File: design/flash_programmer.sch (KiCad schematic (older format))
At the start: 27 parts, among them P1 ISP, U1 MAX662A, U2 2N3906, U3 ATMEGA328P_TQFN, U4 GLS27SF010, U5 74HC595, U6 74HC595

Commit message: Redo PCB: fix errors and shrink
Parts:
- removed R6, R8: 10k, Resistors_SMD:R_0805_HandSoldering, symbol R
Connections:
- net labels added: UNUSED_GND
- wire segments 170 -> 163
- no-connect marks 1 -> 2
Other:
- moved on the sheet: R1, R7

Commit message: Work in progress: Add `12V capability to A9
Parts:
- removed C1, C2: 22nF, Capacitors_SMD:C_0805_HandSoldering, symbol C
- removed C3, C5: 4.7uF, Capacitors_SMD:C_0805_HandSoldering, symbol C
- removed C8: 120nF, Capacitors_SMD:C_0805_HandSoldering, symbol C
- removed D1: LED, LEDs:LED_0805, symbol LED
- removed R2: 150, Resistors_SMD:R_0805_HandSoldering, symbol R
- removed R4: 10k, Resistors_SMD:R_0805_HandSoldering, symbol R
- removed U1: MAX662A, Housings_SOIC:SOIC-8_3.9x4.9mm_Pitch1.27mm, symbol MAX662A
- removed U2: 2N3906, TO_SOT_Packages_SMD:SOT-23_Handsoldering, symbol 2N3906
- removed U4: GLS27SF010, Housings_DIP:DIP-32_W15.24mm, symbol GLS27SF010
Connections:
- net labels added: D[0..7]
- net labels removed: VPP
- wire segments 163 -> 100
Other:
- note removed: "12V Step Up Voltage Supply"
- note removed: "Bypass capacitors for GLS27SF010"
- note removed: "Bypass capacitors for MAX662A"
- note removed: "Flash ROM under read/write"
- note removed: "Write indicator light"
- moved on the sheet: D2, P1, R3

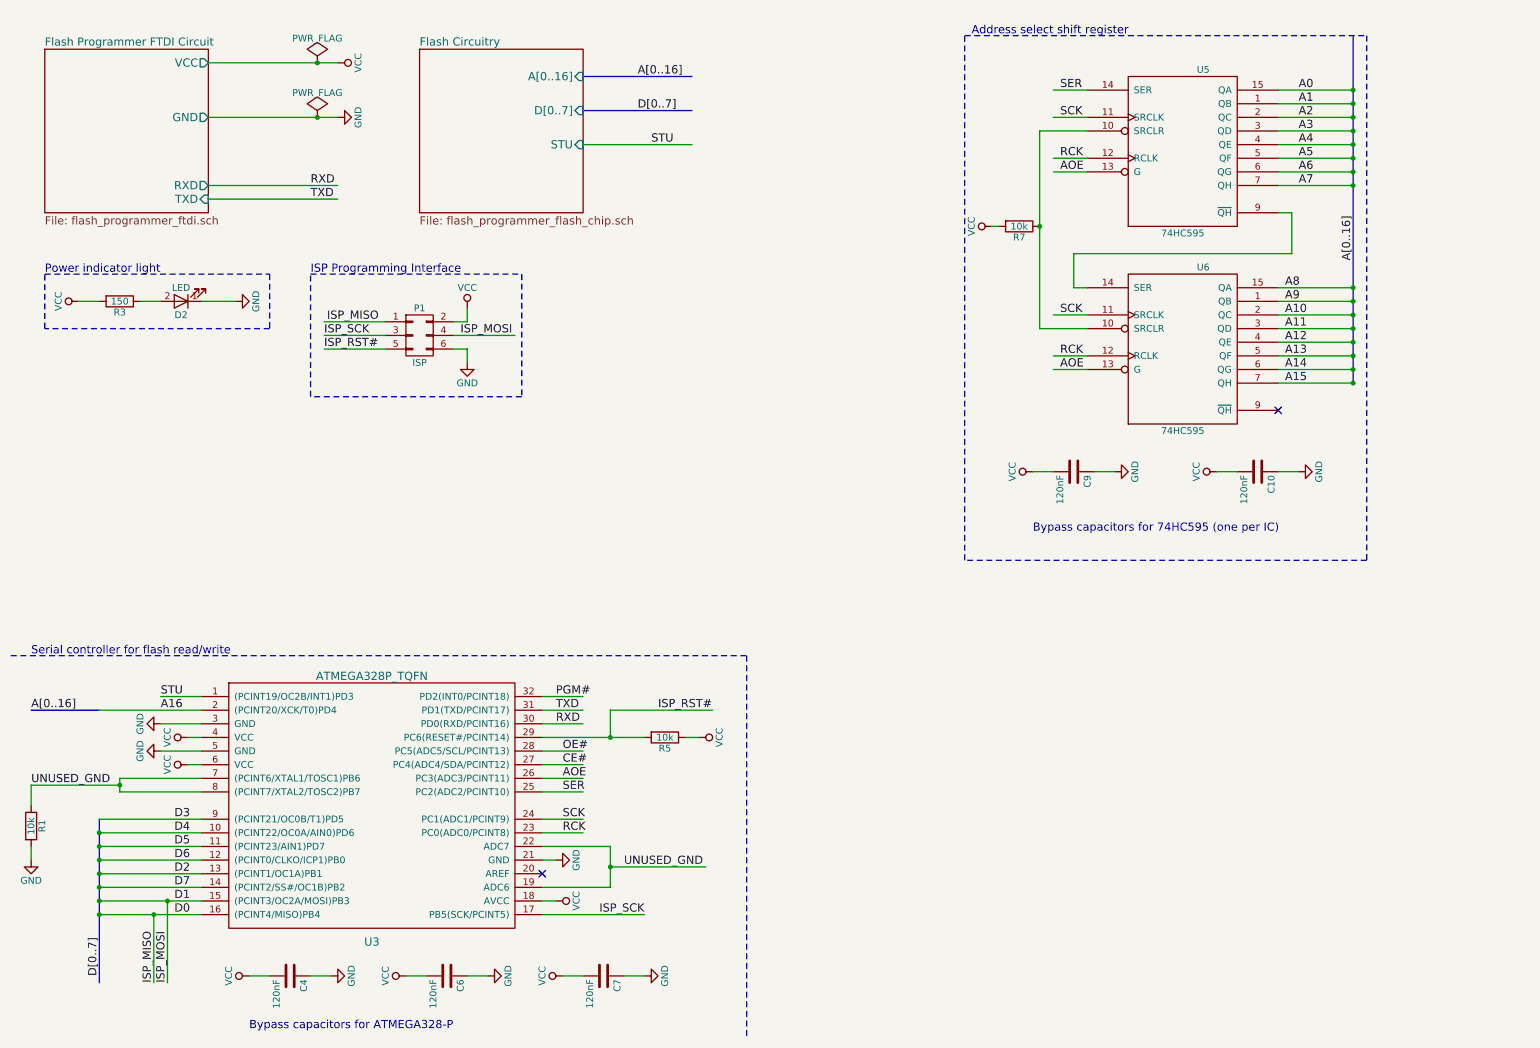
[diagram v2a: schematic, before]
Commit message: Redo the A9_P circuit with a P-channel MOSFET to avoid voltage drop
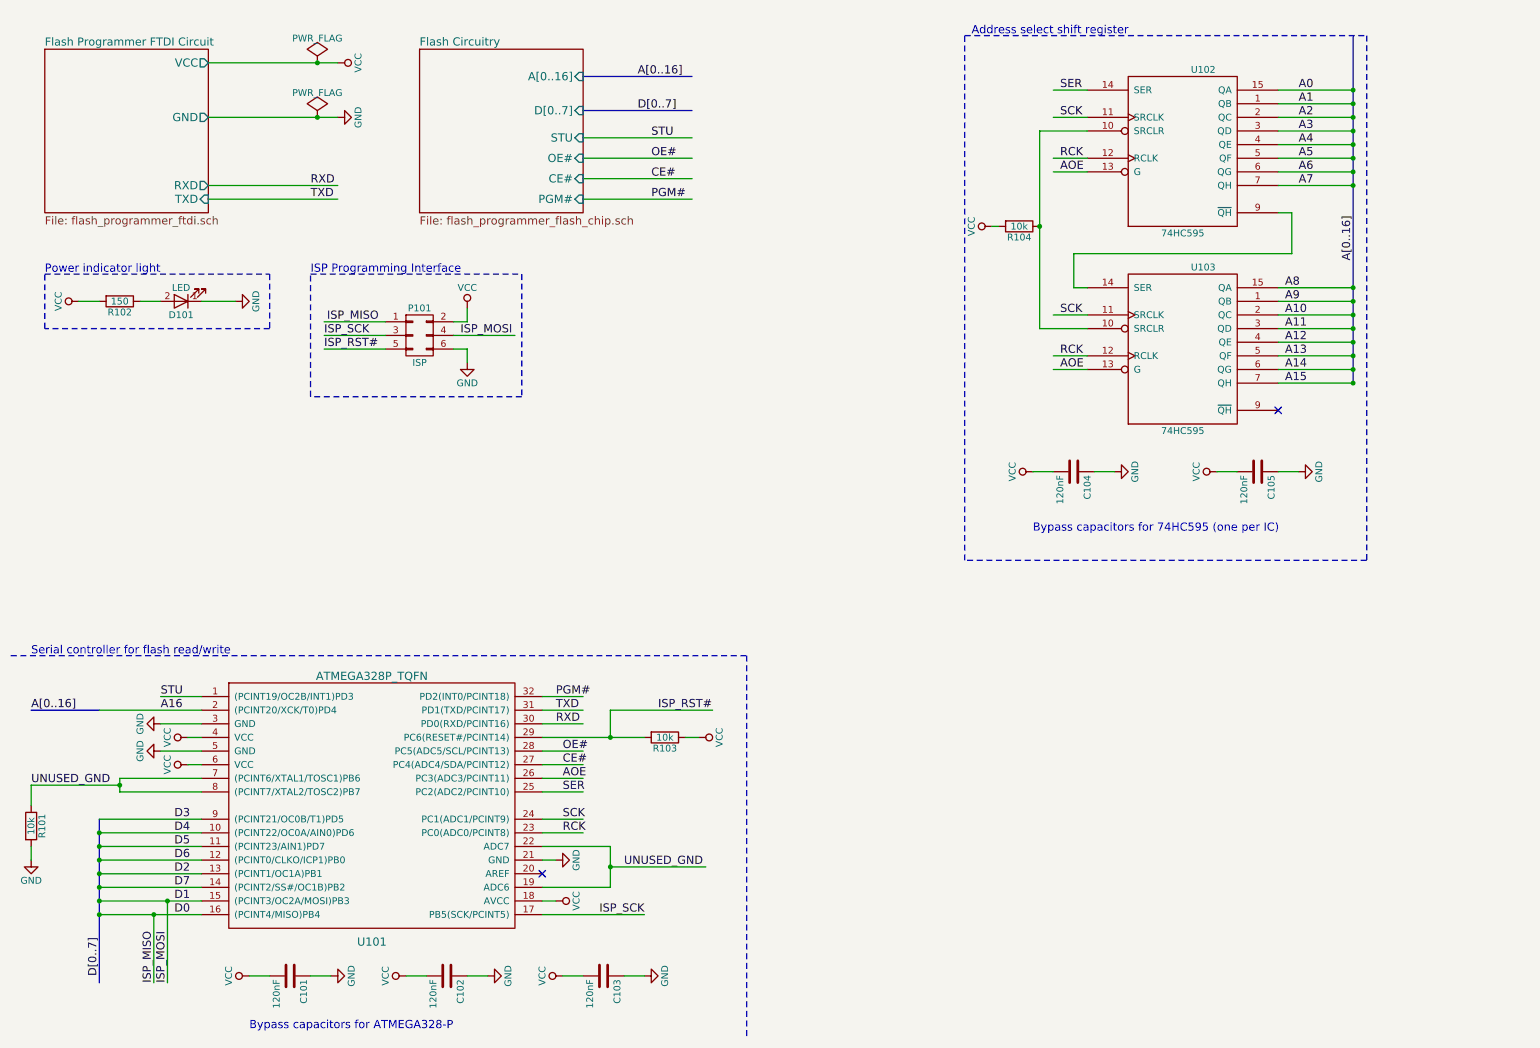
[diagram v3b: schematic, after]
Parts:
- renumbered C4 to C101, C6 to C102, C7 to C103, C9 to C104, C10 to C105, D2 to D101, P1 to P101, R1 to R101, R3 to R102, R5 to R103, R7 to R104, U3 to U101, U5 to U102, U6 to U103
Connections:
- wire segments 100 -> 103
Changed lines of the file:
@@
 $EndDescr
 $Comp
-L 74HC595 U5
+L 74HC595 U102
 U 1 1 5861865E
 P 9100 1500
-F 0 "U5" H 9250 2100 50  0000 C CNN
+F 0 "U102" H 9250 2100 50  0000 C CNN
 F 1 "74HC595" H 9100 900 50  0000 C CNN
 F 2 "Housings_SOIC:SOIC-16_3.9x9.9mm_Pitch1.27mm" H 9100 1500 50  0001 C CNN
@@
 $EndComp
 $Comp
-L 74HC595 U6
+L 74HC595 U103
 U 1 1 586186AF
 P 9100 2950
-F 0 "U6" H 9250 3550 50  0000 C CNN
+F 0 "U103" H 9250 3550 50  0000 C CNN
 F 1 "74HC595" H 9100 2350 50  0000 C CNN
 F 2 "Housings_SOIC:SOIC-16_3.9x9.9mm_Pitch1.27mm" H 9100 2950 50  0001 C CNN
@@
 RXD
 $Comp
-L C C4
+L C C101
 U 1 1 5861E696
 P 2550 7550
-F 0 "C4" H 2575 7650 50  0000 L CNN
+F 0 "C101" H 2575 7650 50  0000 L CNN
 F 1 "120nF" H 2575 7450 50  0000 L CNN
 F 2 "Capacitors_SMD:C_0805_HandSoldering" H 2588 7400 50  0001 C CNN
@@
 $EndComp
 $Comp
-L C C6
+L C C102
 U 1 1 5861E6C9
 P 3700 7550
-F 0 "C6" H 3725 7650 50  0000 L CNN
+F 0 "C102" H 3725 7650 50  0000 L CNN
 F 1 "120nF" H 3725 7450 50  0000 L CNN
 F 2 "Capacitors_SMD:C_0805_HandSoldering" H 3738 7400 50  0001 C CNN
@@
 RCK
 $Comp
-L R R7
+L R R104
 U 1 1 58622531
 P 7900 2050
-F 0 "R7" V 7980 2050 50  0000 C CNN
+F 0 "R104" V 7980 2050 50  0000 C CNN
 F 1 "10k" V 7900 2050 50  0000 C CNN
 F 2 "Resistors_SMD:R_0805_HandSoldering" V 7830 2050 50  0001 C CNN
@@
 A15
 $Comp
-L R R5
+L R R103
 U 1 1 58627FBC
 P 5300 5800
-F 0 "R5" V 5380 5800 50  0000 C CNN
+F 0 "R103" V 5380 5800 50  0000 C CNN
 F 1 "10k" V 5300 5800 50  0000 C CNN
 F 2 "Resistors_SMD:R_0805_HandSoldering" V 5230 5800 50  0001 C CNN
@@
 Connection ~ 10350 2600
 $Comp
-L C C9
+L C C104
 U 1 1 58633F2E
 P 8300 3850
-F 0 "C9" H 8325 3950 50  0000 L CNN
+F 0 "C104" H 8325 3950 50  0000 L CNN
 F 1 "120nF" H 8325 3750 50  0000 L CNN
 F 2 "Capacitors_SMD:C_0805_HandSoldering" H 8338 3700 50  0001 C CNN
@@
 $EndComp
 $Comp
-L GND #PWR09
+L GND #PWR07
 U 1 1 58633F3A
 P 8600 3850
-F 0 "#PWR09" H 8600 3600 50  0001 C CNN
+F 0 "#PWR07" H 8600 3600 50  0001 C CNN
 F 1 "GND" H 8600 3700 50  0000 C CNN
 F 2 "" H 8600 3850 50  0000 C CNN
@@
 $EndComp
 $Comp
-L VCC #PWR011
+L VCC #PWR08
 U 1 1 58633F46
 P 8000 3850
-F 0 "#PWR011" H 8000 3700 50  0001 C CNN
+F 0 "#PWR08" H 8000 3700 50  0001 C CNN
 F 1 "VCC" H 8000 4000 50  0000 C CNN
 F 2 "" H 8000 3850 50  0000 C CNN
@@
 	8450 3850 8600 3850
 $Comp
-L PWR_FLAG #FLG017
+L PWR_FLAG #FLG09
 U 1 1 5864E047
 P 2750 1250
-F 0 "#FLG017" H 2750 1345 50  0001 C CNN
+F 0 "#FLG09" H 2750 1345 50  0001 C CNN
 F 1 "PWR_FLAG" H 2750 1430 50  0000 C CNN
 F 2 "" H 2750 1250 50  0000 C CNN
@@
 $EndComp
 $Comp
-L PWR_FLAG #FLG018
+L PWR_FLAG #FLG010
 U 1 1 5864FE90
 P 2750 850
-F 0 "#FLG018" H 2750 945 50  0001 C CNN
+F 0 "#FLG010" H 2750 945 50  0001 C CNN
 F 1 "PWR_FLAG" H 2750 1030 50  0000 C CNN
 F 2 "" H 2750 850 50  0000 C CNN
@@
 $EndComp
 $Comp
-L GND #PWR019
+L GND #PWR011
 U 1 1 586500D2
 P 2900 1250
-F 0 "#PWR019" H 2900 1000 50  0001 C CNN
+F 0 "#PWR011" H 2900 1000 50  0001 C CNN
 F 1 "GND" H 2900 1100 50  0000 C CNN
 F 2 "" H 2900 1250 50  0000 C CNN
@@
 $EndComp
 $Comp
-L VCC #PWR020
+L VCC #PWR012
 U 1 1 5865011C
 P 2900 850
-F 0 "#PWR020" H 2900 700 50  0001 C CNN
+F 0 "#PWR012" H 2900 700 50  0001 C CNN
 F 1 "VCC" H 2900 1000 50  0000 C CNN
 F 2 "" H 2900 850 50  0000 C CNN
@@
 Address select shift register
 $Comp
-L LED D2
+L LED D101
 U 1 1 5865E22B
 P 1750 2600
-F 0 "D2" H 1750 2700 50  0000 C CNN
+F 0 "D101" H 1750 2700 50  0000 C CNN
 F 1 "LED" H 1750 2500 50  0000 C CNN
 F 2 "LEDs:LED_0805" H 1750 2600 50  0001 C CNN
@@
 $EndComp
 $Comp
-L R R3
+L R R102
 U 1 1 5865E231
 P 1300 2600
-F 0 "R3" V 1380 2600 50  0000 C CNN
+F 0 "R102" V 1380 2600 50  0000 C CNN
 F 1 "150" V 1300 2600 50  0000 C CNN
 F 2 "Resistors_SMD:R_0805_HandSoldering" V 1230 2600 50  0001 C CNN
@@
 	1900 2600 2150 2600
 $Comp
-L GND #PWR022
+L GND #PWR013
 U 1 1 5865E239
 P 2150 2600
-F 0 "#PWR022" H 2150 2350 50  0001 C CNN
+F 0 "#PWR013" H 2150 2350 50  0001 C CNN
 F 1 "GND" H 2150 2450 50  0000 C CNN
 F 2 "" H 2150 2600 50  0000 C CNN
@@
 $EndComp
 $Comp
-L VCC #PWR023
+L VCC #PWR014
 U 1 1 5865E25E
 P 1000 2600
-F 0 "#PWR023" H 1000 2450 50  0001 C CNN
+F 0 "#PWR014" H 1000 2450 50  0001 C CNN
 F 1 "VCC" H 1000 2750 50  0000 C CNN
 F 2 "" H 1000 2600 50  0000 C CNN
@@
 TXD
 $Comp
-L CONN_02X03 P1
+L CONN_02X03 P101
 U 1 1 588F8D78
 P 3500 2850
-F 0 "P1" H 3500 3050 50  0000 C CNN
+F 0 "P101" H 3500 3050 50  0000 C CNN
 F 1 "ISP" H 3500 2650 50  0000 C CNN
 F 2 "Pin_Headers:Pin_Header_Straight_2x03_Pitch2.54mm" H 3500 1650 50  0001 C CNN
@@
 	3850 2950 3850 3050
 $Comp
-L VCC #PWR026
+L VCC #PWR015
 U 1 1 588FF450
 P 3850 2650
-F 0 "#PWR026" H 3850 2500 50  0001 C CNN
+F 0 "#PWR015" H 3850 2500 50  0001 C CNN
 F 1 "VCC" H 3850 2800 50  0000 C CNN
 F 2 "" H 3850 2650 50  0000 C CNN
@@
 $EndComp
 $Comp
-L GND #PWR027
+L GND #PWR016
 U 1 1 588FF4D9
 P 3850 3050
-F 0 "#PWR027" H 3850 2800 50  0001 C CNN
+F 0 "#PWR016" H 3850 2800 50  0001 C CNN
 F 1 "GND" H 3850 2900 50  0000 C CNN
 F 2 "" H 3850 3050 50  0000 C CNN
@@
 ISP Programming Interface
 $Comp
-L ATMEGA328P_TQFN U3
+L ATMEGA328P_TQFN U101
 U 1 1 589256D2
 P 3150 7200
-F 0 "U3" H 3150 7100 60  0000 C CNN
+F 0 "U101" H 3150 7100 60  0000 C CNN
 F 1 "ATMEGA328P_TQFN" H 3150 9050 60  0000 C CNN
 F 2 "TQFP_32_7mm_0.8mm_pitch:TQFP-32" H 3100 7200 60  0001 C CNN
@@
 	1900 6000 1800 6000
 $Comp
-L VCC #PWR028
+L VCC #PWR017
 U 1 1 58927B2C
 P 1800 6000
-F 0 "#PWR028" H 1800 5850 50  0001 C CNN
+F 0 "#PWR017" H 1800 5850 50  0001 C CNN
 F 1 "VCC" H 1800 6150 50  0000 C CNN
 F 2 "" H 1800 6000 50  0000 C CNN
@@
 $EndComp
 $Comp
-L VCC #PWR029
+L VCC #PWR018
 U 1 1 58927F01
 P 1800 5800
-F 0 "#PWR029" H 1800 5650 50  0001 C CNN
+F 0 "#PWR018" H 1800 5650 50  0001 C CNN
 F 1 "VCC" H 1800 5950 50  0000 C CNN
 F 2 "" H 1800 5800 50  0000 C CNN
@@
 $EndComp
 $Comp
-L GND #PWR030
+L GND #PWR019
 U 1 1 589283EC
 P 1600 5900
-F 0 "#PWR030" H 1600 5650 50  0001 C CNN
+F 0 "#PWR019" H 1600 5650 50  0001 C CNN
 F 1 "GND" H 1600 5750 50  0000 C CNN
 F 2 "" H 1600 5900 50  0000 C CNN
@@
 $EndComp
 $Comp
-L GND #PWR031
+L GND #PWR020
 U 1 1 58928850
 P 1600 5700
-F 0 "#PWR031" H 1600 5450 50  0001 C CNN
+F 0 "#PWR020" H 1600 5450 50  0001 C CNN
 F 1 "GND" H 1600 5550 50  0000 C CNN
 F 2 "" H 1600 5700 50  0000 C CNN
@@
 $EndComp
 $Comp
-L GND #PWR032
+L GND #PWR021
 U 1 1 5892A371
 P 4500 6700
-F 0 "#PWR032" H 4500 6450 50  0001 C CNN
+F 0 "#PWR021" H 4500 6450 50  0001 C CNN
 F 1 "GND" H 4500 6550 50  0000 C CNN
 F 2 "" H 4500 6700 50  0000 C CNN
@@
 $EndComp
 $Comp
-L VCC #PWR033
+L VCC #PWR022
 U 1 1 5892A3F7
 P 4500 7000
-F 0 "#PWR033" H 4500 6850 50  0001 C CNN
+F 0 "#PWR022" H 4500 6850 50  0001 C CNN
 F 1 "VCC" H 4500 7150 50  0000 C CNN
 F 2 "" H 4500 7000 50  0000 C CNN
@@
 RCK
 $Comp
-L R R1
+L R R101
 U 1 1 589374D9
 P 650 6450
-F 0 "R1" V 730 6450 50  0000 C CNN
+F 0 "R101" V 730 6450 50  0000 C CNN
 F 1 "10k" V 650 6450 50  0000 C CNN
 F 2 "Resistors_SMD:R_0805_HandSoldering" V 580 6450 50  0001 C CNN
@@
 	650  6600 650  6700
 $Comp
-L GND #PWR034
+L GND #PWR023
 U 1 1 58937CB7
 P 650 6700
-F 0 "#PWR034" H 650 6450 50  0001 C CNN
+F 0 "#PWR023" H 650 6450 50  0001 C CNN
 F 1 "GND" H 650 6550 50  0000 C CNN
 F 2 "" H 650 6700 50  0000 C CNN
@@
 	7500 4500 7500 650
 $Comp
-L C C10
+L C C105
 U 1 1 5895932D
 P 9650 3850
-F 0 "C10" H 9675 3950 50  0000 L CNN
+F 0 "C105" H 9675 3950 50  0000 L CNN
 F 1 "120nF" H 9675 3750 50  0000 L CNN
 F 2 "Capacitors_SMD:C_0805_HandSoldering" H 9688 3700 50  0001 C CNN
@@
 $EndComp
 $Comp
-L GND #PWR035
+L GND #PWR024
 U 1 1 58959333
 P 9950 3850
-F 0 "#PWR035" H 9950 3600 50  0001 C CNN
+F 0 "#PWR024" H 9950 3600 50  0001 C CNN
 F 1 "GND" H 9950 3700 50  0000 C CNN
 F 2 "" H 9950 3850 50  0000 C CNN
@@
 $EndComp
 $Comp
-L VCC #PWR036
+L VCC #PWR025
 U 1 1 58959339
 P 9350 3850
-F 0 "#PWR036" H 9350 3700 50  0001 C CNN
+F 0 "#PWR025" H 9350 3700 50  0001 C CNN
 F 1 "VCC" H 9350 4000 50  0000 C CNN
 F 2 "" H 9350 3850 50  0000 C CNN
@@
 Bypass capacitors for 74HC595 (one per IC)
 $Comp
-L C C7
+L C C103
 U 1 1 58976DF8
 P 4850 7550
-F 0 "C7" H 4875 7650 50  0000 L CNN
+F 0 "C103" H 4875 7650 50  0000 L CNN
 F 1 "120nF" H 4875 7450 50  0000 L CNN
 F 2 "Capacitors_SMD:C_0805_HandSoldering" H 4888 7400 50  0001 C CNN
@@
 $EndComp
 $Comp
-L GND #PWR037
+L GND #PWR026
 U 1 1 58976DFE
 P 5150 7550
-F 0 "#PWR037" H 5150 7300 50  0001 C CNN
+F 0 "#PWR026" H 5150 7300 50  0001 C CNN
 F 1 "GND" H 5150 7400 50  0000 C CNN
 F 2 "" H 5150 7550 50  0000 C CNN
@@
 $EndComp
 $Comp
-L VCC #PWR038
+L VCC #PWR027
 U 1 1 58976E04
 P 4550 7550
-F 0 "#PWR038" H 4550 7400 50  0001 C CNN
+F 0 "#PWR027" H 4550 7400 50  0001 C CNN
 F 1 "VCC" H 4550 7700 50  0000 C CNN
 F 2 "" H 4550 7550 50  0000 C CNN
@@
 F2 "A[0..16]" I R 4700 950 60
 F3 "D[0..7]" I R 4700 1200 60
-F4 "STU" I R 4700 1450 60
+F4 "STU" I R 4700 1400 60
+F5 "OE#" I R 4700 1550 60
+F6 "CE#" I R 4700 1700 60
+F7 "PGM#" I R 4700 1850 60
 $EndSheet
 Wire Bus Line
@@
 A[0..16]
 Wire Wire Line
-	4700 1450 5500 1450
-Text Label 5200 1450 0    60   ~ 0
+	4700 1400 5500 1400
+Text Label 5200 1400 0    60   ~ 0
 STU
+Wire Wire Line
+	4700 1550 5500 1550
+Wire Wire Line
+	4700 1700 5500 1700
+Wire Wire Line
+	4700 1850 5500 1850
+Text Label 5200 1550 0    60   ~ 0
+OE#
+Text Label 5200 1700 0    60   ~ 0
+CE#
+Text Label 5200 1850 0    60   ~ 0
+PGM#
 $EndSCHEMATC

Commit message: Redraw schematic for clarity
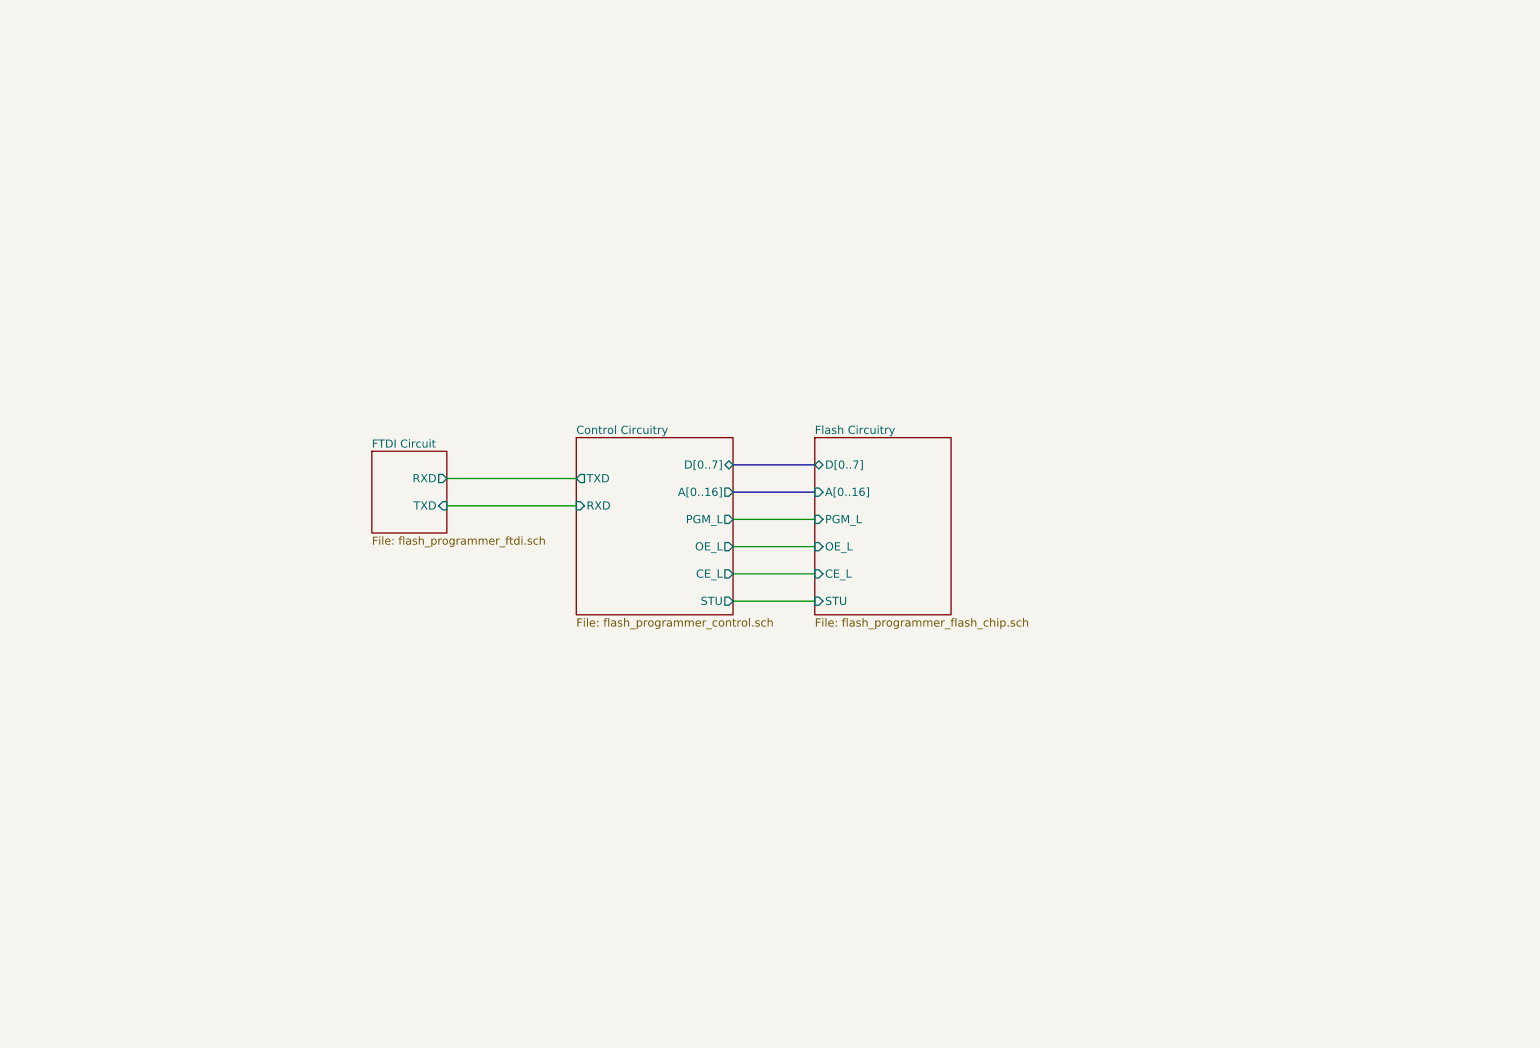
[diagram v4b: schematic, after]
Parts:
- removed C101, C102, C103, C104, C105: 120nF, Capacitors_SMD:C_0805_HandSoldering, symbol C
- removed D101: LED, LEDs:LED_0805, symbol LED
- removed P101: ISP, Pin_Headers:Pin_Header_Straight_2x03_Pitch2.54mm, symbol CONN_02X03
- removed R101, R103, R104: 10k, Resistors_SMD:R_0805_HandSoldering, symbol R
- removed R102: 150, Resistors_SMD:R_0805_HandSoldering, symbol R
- removed U101: ATMEGA328P_TQFN, TQFP_32_7mm_0.8mm_pitch:TQFP-32, symbol ATMEGA328P_TQFN
- removed U102, U103: 74HC595, Housings_SOIC:SOIC-16_3.9x9.9mm_Pitch1.27mm, symbol 74HC595
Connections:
- net labels removed: A0, A1, A10, A11, A12, A13, A14, A15, A16, A2, A3, A4, A5, A6, A7, A8, A9, AOE, A[0..16], CE#, D0, D1, D2, D3, D4, D5, D6, D7, D[0..7], GND, ISP_MISO, ISP_MOSI, ISP_RST#, ISP_SCK, OE#, PGM#, RCK, RXD, SCK, SER, STU, TXD, UNUSED_GND, VCC
- wire segments 103 -> 6
- no-connect marks 2 -> 0
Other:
- note removed: "Address select shift register"
- note removed: "Bypass capacitors for 74HC595 (one per IC)"
- note removed: "Bypass capacitors for ATMEGA328-P"
- note removed: "ISP Programming Interface"
- note removed: "Power indicator light"
- note removed: "Serial controller for flash read/write"
